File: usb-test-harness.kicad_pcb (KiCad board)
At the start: 4 copper layers, 85 x 73 mm, 87 parts, among them J1 5V_RAW, J10 USB_A_DUAL, J2 GND, J3 V_EXT, J4 USB_A (female down), J5 Conn_01x03_Male, J6 USB_A_DUAL, J7 USB_A_DUAL, J8 USB_A (male up), J9 USB_B_Micro (up), U1 FT24C02A, U2 SE5120ST33, U3 USB2517, U4 APL3511C, U5 APL3511C, U6 APL3511C, U7 APL3511C, U8 APL3511C, U9 APL3511C, Y1 24MHz

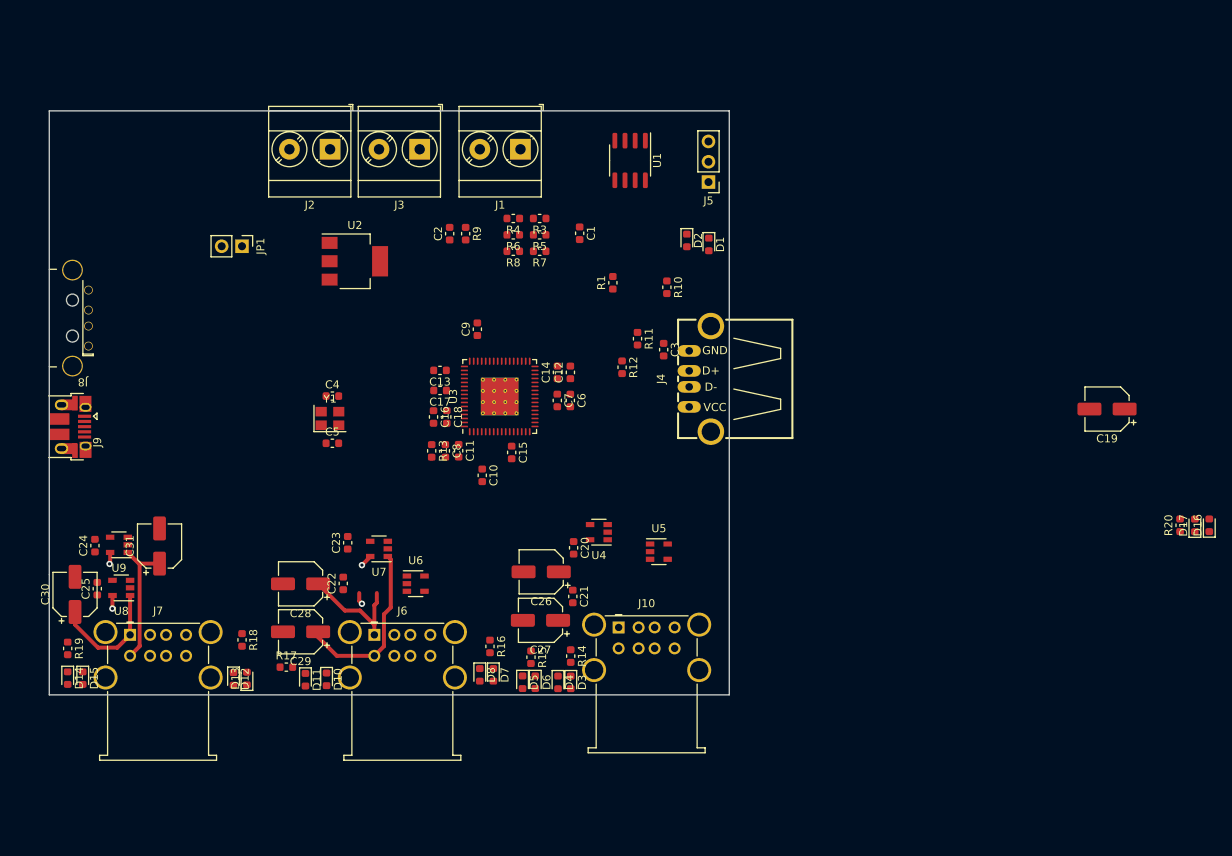
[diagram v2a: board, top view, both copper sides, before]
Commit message: usb hub: choose a box, redraw frame
Closer and closer
Now we have an enclosure: https://www.tme.eu/is/en/details/abs-35/enclosures-with-panel/maszczyk/km-35-gy/
Set up the holes and outline properly.  Now we can really get started.
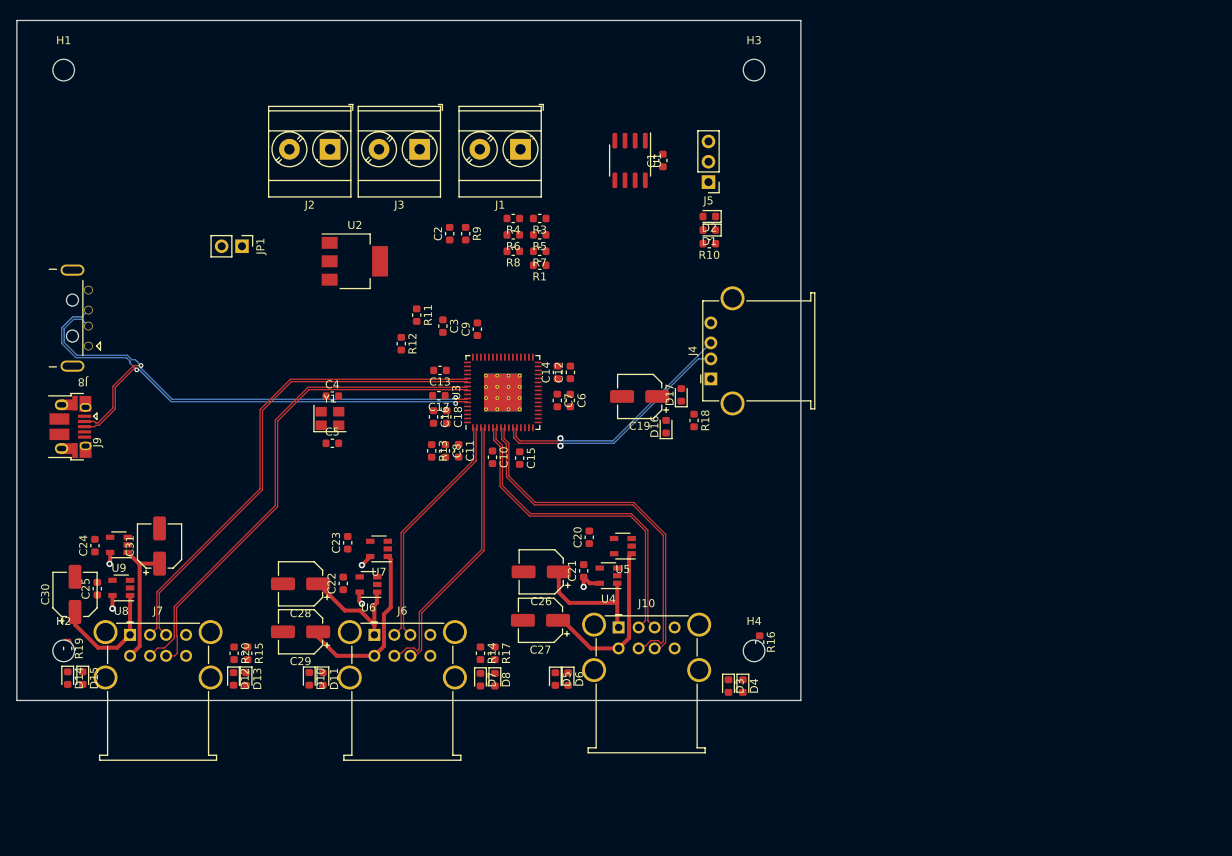
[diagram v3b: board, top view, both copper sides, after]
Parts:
- added H1: MountingHole, MountingHole:MountingHole_2.7mm_M2.5, F.Cu at (105.1, 56.8)
- added H2: MountingHole, MountingHole:MountingHole_2.7mm_M2.5, F.Cu at (105.1, 129.4)
- added H3: MountingHole, MountingHole:MountingHole_2.7mm_M2.5, F.Cu at (191.4, 56.8)
- added H4: MountingHole, MountingHole:MountingHole_2.7mm_M2.5, F.Cu at (191.4, 129.4)
- D16: value G7 -> G7_DS
- D17: value R7 -> R7_DS
- J4: footprint OPL_Connector:USB4+2P-2.0-90D -> Connector_USB:USB_A_Stewart_SS-52100-001_Horizontal
- J8: value USB_A (male up) -> USB_A SOFNG USB-05
- moved R20 119.3 mm to (126.4, 129.7), turned to -90 degrees
- moved D16 69.0 mm to (180.4, 101.4)
- moved D17 66.2 mm to (182.3, 97.4)
- moved R18 62.8 mm to (183.9, 100.6)
- moved C19 58.4 mm to (177.1, 97.6)
- moved R15 35.4 mm to (128.1, 129.7)
- moved R16 33.7 mm to (192.1, 128.3)
- moved R11 27.8 mm to (149.2, 87.4)
- moved C3 27.8 mm to (152.5, 88.8)
- moved R12 27.8 mm to (147.3, 91.0)
- moved R17 26.1 mm to (159.0, 129.7), turned to -90 degrees
- moved D4 23.1 mm to (190.0, 133.8)
- moved D3 19.7 mm to (188.2, 133.8)
- moved C1 13.8 mm to (180.0, 68.1), turned to 90 degrees
- moved R14 11.3 mm to (157.2, 129.7)
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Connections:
- net Net-(D10-Pad2) renamed /upstream-config-leds/LED_DRIVE
- net Net-(R11-Pad2) renamed /upstream-config-leds/VBUS_DET
- D10 pad 1: Net-(D10-Pad1) -> /upstream-config-leds/LA_2-4
- D11 pad 2: Net-(D10-Pad1) -> /upstream-config-leds/LA_2-4
- D12 pad 1: Net-(D12-Pad1) -> /upstream-config-leds/LA7-5
- D13 pad 2: Net-(D12-Pad1) -> /upstream-config-leds/LA7-5
- D14 pad 1: Net-(D14-Pad1) -> /upstream-config-leds/LA5-DS
- D15 pad 2: Net-(D14-Pad1) -> /upstream-config-leds/LA5-DS
- D16 pad 1: Net-(D16-Pad1) -> /upstream-config-leds/LA_6-6
- D17 pad 2: Net-(D16-Pad1) -> /upstream-config-leds/LA_6-6
- D3 pad 1: Net-(D3-Pad1) -> /upstream-config-leds/LA_3-1
- D4 pad 2: Net-(D3-Pad1) -> /upstream-config-leds/LA_3-1
- D5 pad 1: Net-(D5-Pad1) -> /upstream-config-leds/LA_4-2
- D6 pad 2: Net-(D5-Pad1) -> /upstream-config-leds/LA_4-2
- D7 pad 1: Net-(D7-Pad1) -> /upstream-config-leds/LA_1-3
- D8 pad 2: Net-(D7-Pad1) -> /upstream-config-leds/LA_1-3
- R14 pad 2: Net-(D3-Pad1) -> /upstream-config-leds/LA_1-3
- R15 pad 2: Net-(D5-Pad1) -> /upstream-config-leds/LA_2-4
- R16 pad 2: Net-(D7-Pad1) -> /upstream-config-leds/LA_3-1
- R17 pad 2: Net-(D10-Pad1) -> /upstream-config-leds/LA_4-2
- R18 pad 2: Net-(D12-Pad1) -> /upstream-config-leds/LA5-DS
- R19 pad 2: Net-(D14-Pad1) -> /upstream-config-leds/LA_6-6
- R20 pad 2: Net-(D16-Pad1) -> /upstream-config-leds/LA7-5
- U3 pad 36: /downstream-port-power/EN5 -> /downstream-port-power/EN6
- U3 pad 37: /downstream-port-power/OC5 -> /downstream-port-power/OC6
- U3 pad 38: /downstream-port-power/OC6 -> /downstream-port-power/OC5
- U3 pad 39: /downstream-port-power/EN6 -> /downstream-port-power/EN5
- U3 pad 53: /downstream-port-power/U6- -> /downstream-port-power/U5-
- U3 pad 54: /downstream-port-power/U6+ -> /downstream-port-power/U5+
- U3 pad 55: /downstream-port-power/U5- -> /downstream-port-power/U6-
- U3 pad 56: /downstream-port-power/U5+ -> /downstream-port-power/U6+
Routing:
- net /upstream-config-leds/UP+: track 0.00 -> 71.6 mm, vias 0 -> 2
- net /upstream-config-leds/UP-: track 0.00 -> 71.0 mm, vias 0 -> 2
- net /downstream-port-power/U6-: track 0.00 -> 62.2 mm
- net /downstream-port-power/U5-: track 0.00 -> 61.4 mm
- net /downstream-port-power/U6+: track 0.00 -> 61.2 mm
- net /downstream-port-power/U5+: track 0.00 -> 60.9 mm
- net /downstream-port-power/U2-: track 0.00 -> 46.1 mm
- net /downstream-port-power/U2+: track 0.00 -> 44.1 mm
- net /downstream-port-power/U1-: track 0.00 -> 40.6 mm
- net /downstream-port-power/U1+: track 0.00 -> 40.6 mm
- net /downstream-port-power/U4-: track 0.00 -> 34.7 mm
- net /downstream-port-power/U4+: track 0.00 -> 32.8 mm
- net /downstream-port-power/DS+: track 0.00 -> 31.1 mm, vias 0 -> 1
- net /downstream-port-power/DS-: track 0.00 -> 30.9 mm, vias 0 -> 1
- net /downstream-port-power/U3-: track 0.00 -> 30.0 mm
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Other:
- board size 85 x 73 mm -> 98 x 85 mm
- net class usb-4l-2313 added: clearance 0.15, trace_width 0.15, via_dia 0.6, via_drill 0.3
- net class usb-traces-4l removed
- rule trace_min: 0.2 -> 0.1
- board text added: "JLCPCB 2313 stackup!"

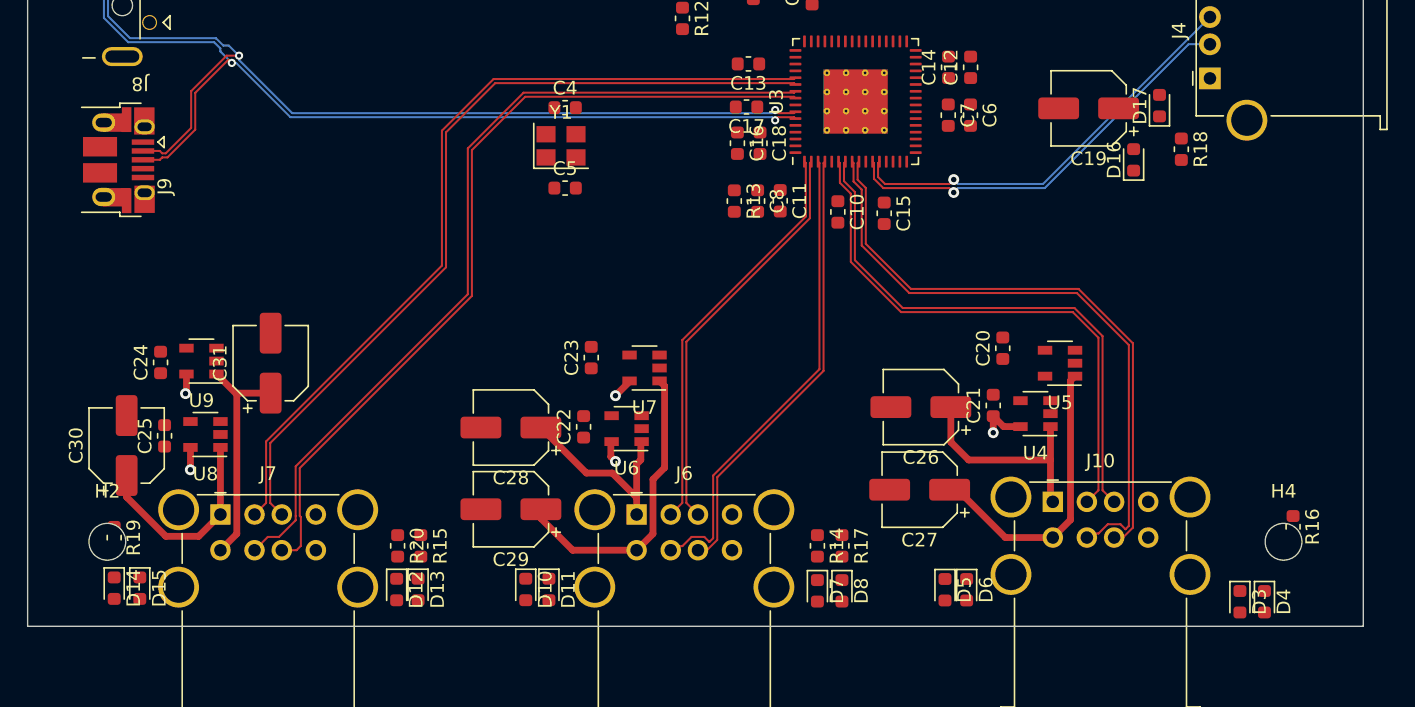
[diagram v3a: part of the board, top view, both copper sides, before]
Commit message: usb-hub: update leds and add footprint for it
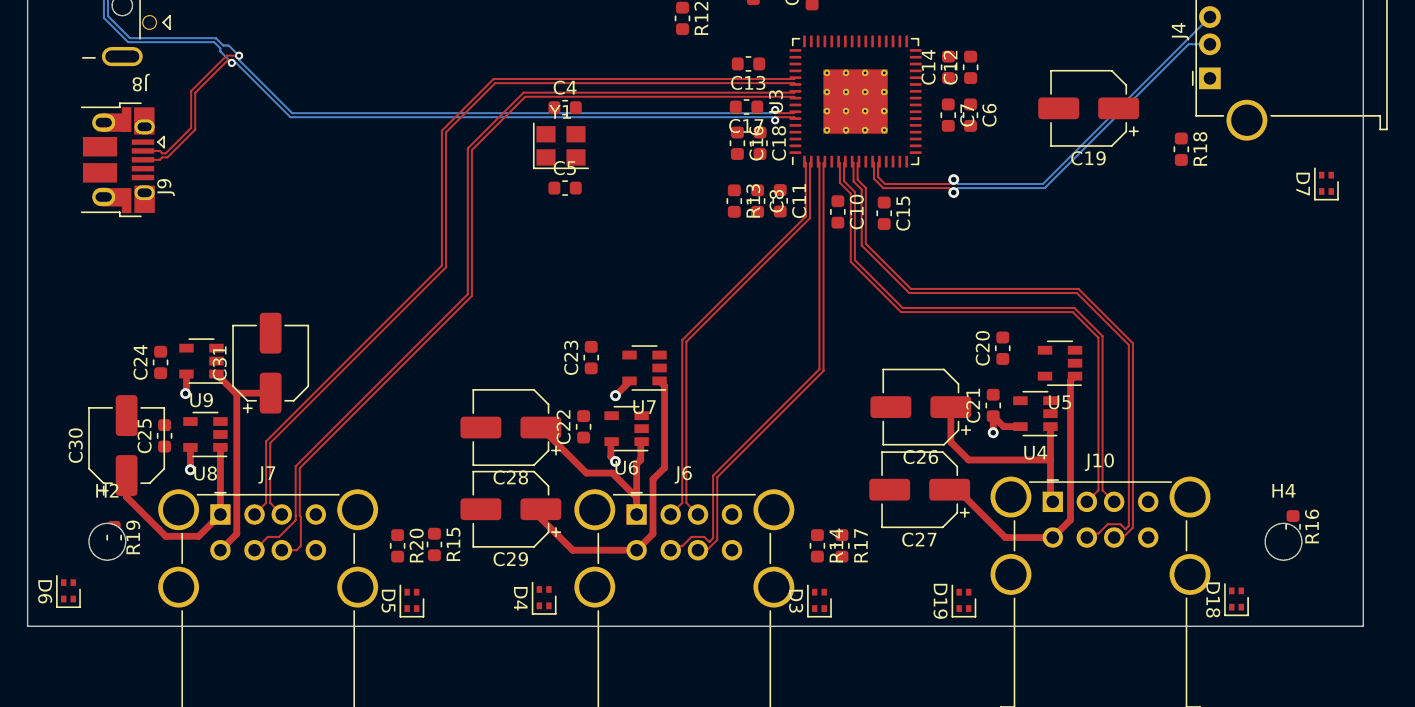
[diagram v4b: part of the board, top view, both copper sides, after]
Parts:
- removed D10: G4, LED_SMD:LED_0603_1608Metric
- removed D11: R4, LED_SMD:LED_0603_1608Metric
- removed D12: G5, LED_SMD:LED_0603_1608Metric
- removed D13: R5, LED_SMD:LED_0603_1608Metric
- removed D14: G6, LED_SMD:LED_0603_1608Metric
- removed D15: R6, LED_SMD:LED_0603_1608Metric
- removed D16: G7_DS, LED_SMD:LED_0603_1608Metric
- removed D17: R7_DS, LED_SMD:LED_0603_1608Metric
- removed D8: R3, LED_SMD:LED_0603_1608Metric
- added D18: LTST-C295KGKRKT, LED_SMD:LED_LiteOn_LTST-C295K, F.Cu at (188.3, 133.0)
- added D19: LTST-C295KGKRKT, LED_SMD:LED_LiteOn_LTST-C295K, F.Cu at (168.3, 133.1)
- D3: value G1 -> LTST-C295KGKRKT; footprint LED_SMD:LED_0603_1608Metric -> LED_SMD:LED_LiteOn_LTST-C295K
- D4: value R1 -> LTST-C295KGKRKT; footprint LED_SMD:LED_0603_1608Metric -> LED_SMD:LED_LiteOn_LTST-C295K
- D5: value G2 -> LTST-C295KGKRKT; footprint LED_SMD:LED_0603_1608Metric -> LED_SMD:LED_LiteOn_LTST-C295K
- D6: value R2 -> LTST-C295KGKRKT; footprint LED_SMD:LED_0603_1608Metric -> LED_SMD:LED_LiteOn_LTST-C295K
- D7: value G3 -> LTST-C295KGKRKT; footprint LED_SMD:LED_0603_1608Metric -> LED_SMD:LED_LiteOn_LTST-C295K
- moved D6 65.6 mm to (102.6, 132.4)
- moved D4 52.5 mm to (137.5, 132.9)
- moved D7 48.5 mm to (194.9, 102.5)
- moved D5 38.8 mm to (127.8, 133.1)
- moved D3 30.5 mm to (157.7, 133.1)
- moved R15 1.00 mm to (129.1, 129.6)
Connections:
- D3 pad 1: /upstream-config-leds/LA_3-1 -> /upstream-config-leds/LED_DRIVE
- D3 pad 2: /upstream-config-leds/LED_DRIVE -> /upstream-config-leds/LA_1-3
- D4 pad 1: GND -> /upstream-config-leds/LED_DRIVE
- D4 pad 2: /upstream-config-leds/LA_3-1 -> /upstream-config-leds/LA_2-4
- D5 pad 1: /upstream-config-leds/LA_4-2 -> /upstream-config-leds/LED_DRIVE
- D5 pad 2: /upstream-config-leds/LED_DRIVE -> /upstream-config-leds/LA_7-5
- D6 pad 1: GND -> /upstream-config-leds/LED_DRIVE
- D6 pad 2: /upstream-config-leds/LA_4-2 -> /upstream-config-leds/LA_6-6
- D7 pad 1: /upstream-config-leds/LA_1-3 -> /upstream-config-leds/LED_DRIVE
- D7 pad 2: /upstream-config-leds/LED_DRIVE -> /upstream-config-leds/LA_5-DS
- R18 pad 2: /upstream-config-leds/LA5-DS -> /upstream-config-leds/LA_5-DS
- R20 pad 2: /upstream-config-leds/LA7-5 -> /upstream-config-leds/LA_7-5

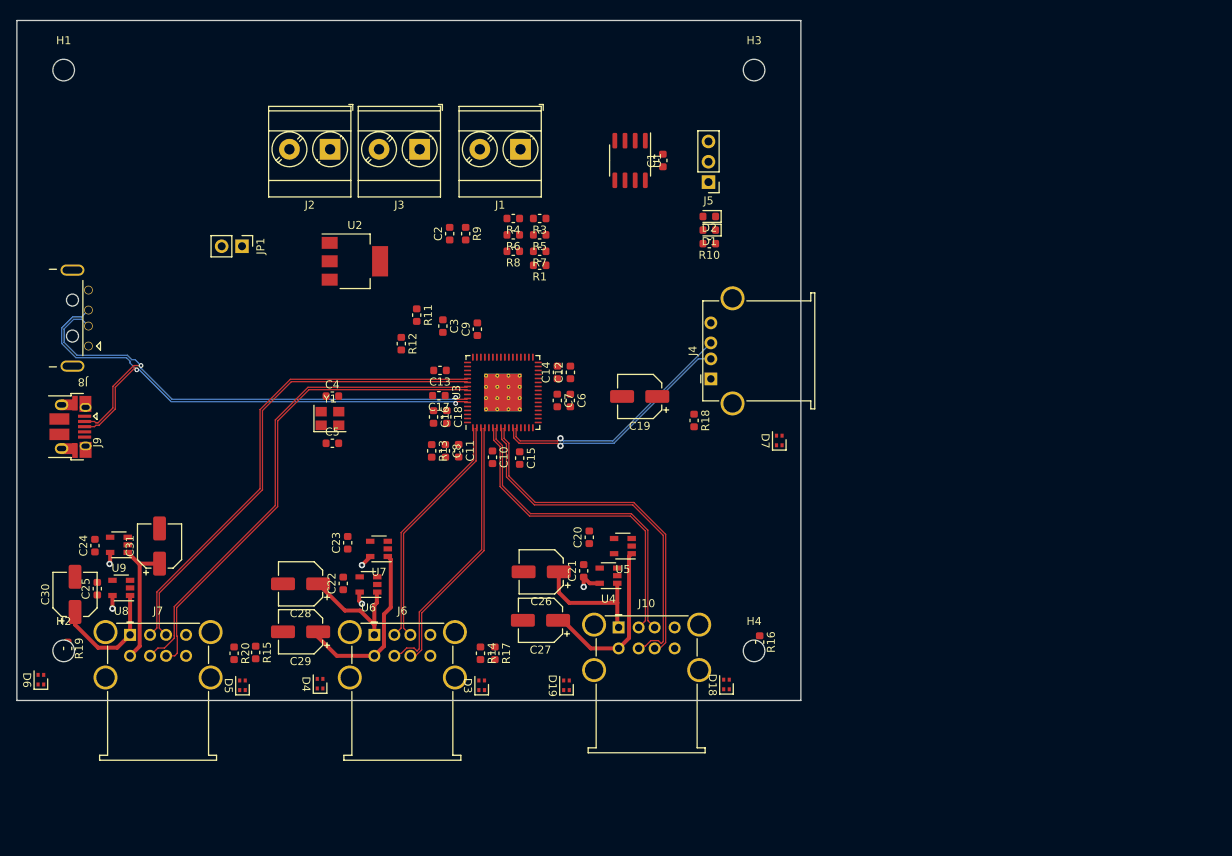
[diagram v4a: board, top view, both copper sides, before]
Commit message: usb-hub: pcb: precisely layout all the connectors again
lock them in place, properly even and nice and clean now.  Now you can
_really_ start routing.
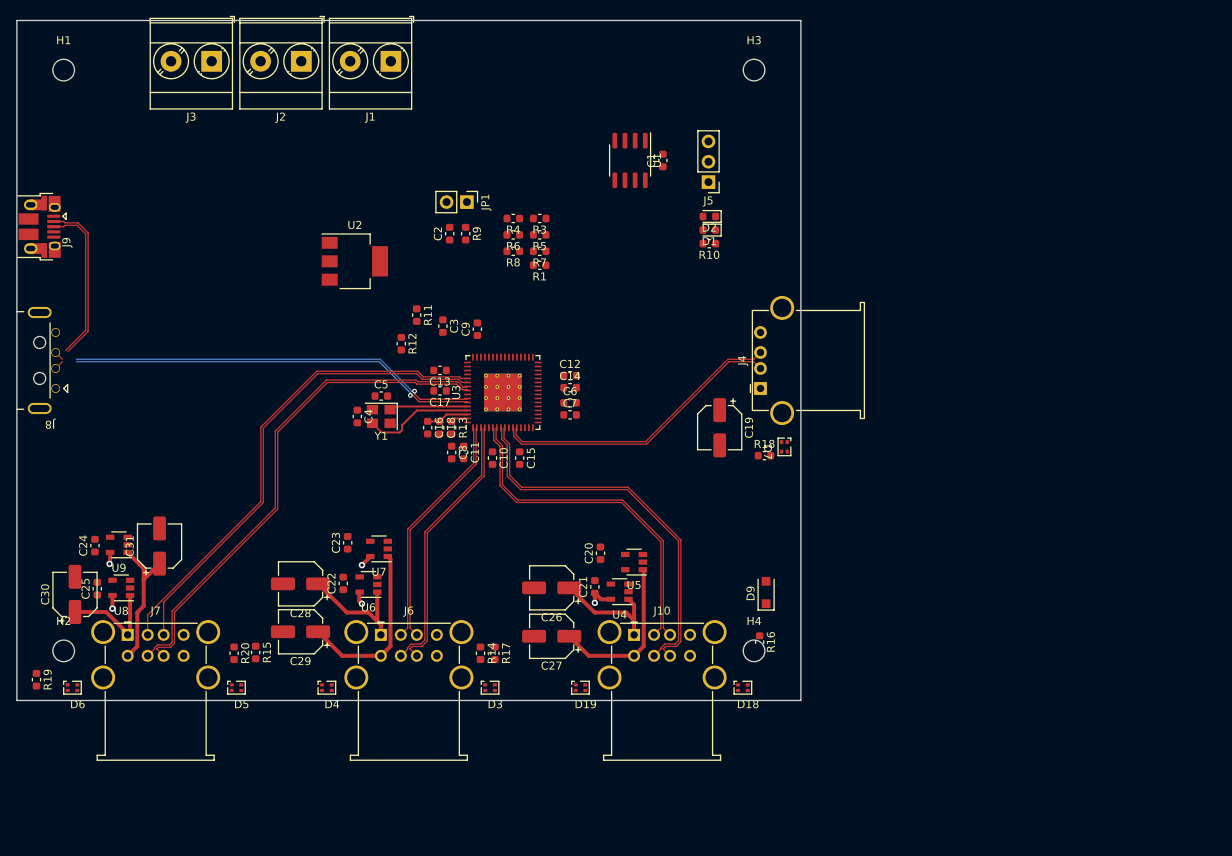
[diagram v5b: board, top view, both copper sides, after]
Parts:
- added D9: D_Small, Diode_SMD:D_SOD-123F, F.Cu at (192.9, 122.1)
- moved JP1 28.6 mm to (155.5, 73.3)
- moved J3 28.2 mm to (123.6, 55.7)
- moved J9 25.3 mm to (102.1, 76.4)
- moved J1 19.6 mm to (146.0, 55.7)
- moved J2 11.6 mm to (134.8, 55.7)
- moved C19 10.7 mm to (187.1, 101.5), turned to -90 degrees
- moved R18 9.84 mm to (192.7, 105.0), turned to 0 degrees
- moved C5 8.50 mm to (144.8, 97.5)
- moved J8 6.70 mm to (102.1, 93.1)
- moved Y1 6.42 mm to (144.8, 100.1), turned to 180 degrees
- moved J4 6.32 mm to (192.2, 96.6)
- moved R19 5.52 mm to (101.7, 133.0)
- moved C4 4.02 mm to (141.8, 100.1), turned to -90 degrees
- moved D6 3.94 mm to (106.2, 134.0), turned to 0 degrees
- moved R13 3.83 mm to (153.6, 101.5)
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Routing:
- net /upstream-config-leds/XTAL1: track 0.00 -> 13.9 mm
- net /upstream-config-leds/XTAL2: track 0.00 -> 9.85 mm
- net /downstream-port-power/DS-: track 30.9 -> 37.0 mm, vias 1 -> 0
- net /downstream-port-power/DS+: track 31.1 -> 36.5 mm, vias 1 -> 0
- net /upstream-config-leds/VDD18PLL: track 0.00 -> 5.34 mm
- net /downstream-port-power/U2+: track 44.1 -> 47.5 mm
- net /downstream-port-power/VBUS5: track 15.2 -> 12.9 mm
- net /upstream-config-leds/RBIAS: track 0.00 -> 2.14 mm
- net /upstream-config-leds/UP-: track 71.0 -> 73.1 mm, vias 2 -> 1
- net /downstream-port-power/U1+: track 40.6 -> 42.6 mm
- net /downstream-port-power/U1-: track 40.6 -> 42.6 mm
- net /downstream-port-power/VBUS1: track 16.0 -> 14.4 mm
- net /downstream-port-power/U2-: track 46.1 -> 47.5 mm
- net /downstream-port-power/U4-: track 34.7 -> 33.4 mm
- net /downstream-port-power/VBUS2: track 21.5 -> 20.4 mm
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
